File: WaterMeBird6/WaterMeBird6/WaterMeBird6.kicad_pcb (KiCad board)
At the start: 2 copper layers, 13 parts, among them J2 Conn_01x03, Q1 2N3904, SW1 SW_Push, U1 ATtiny85V-10P

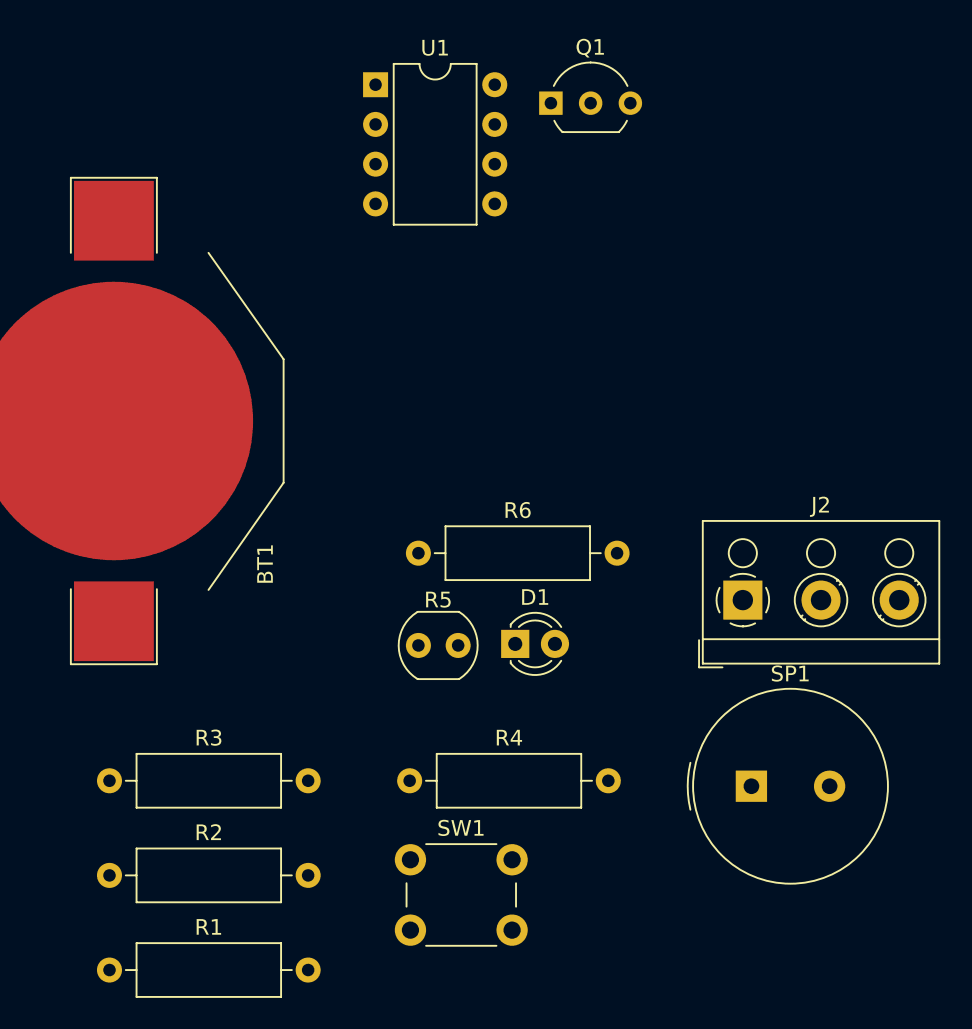
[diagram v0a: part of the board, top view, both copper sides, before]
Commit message: Added 'thick' version of footprints
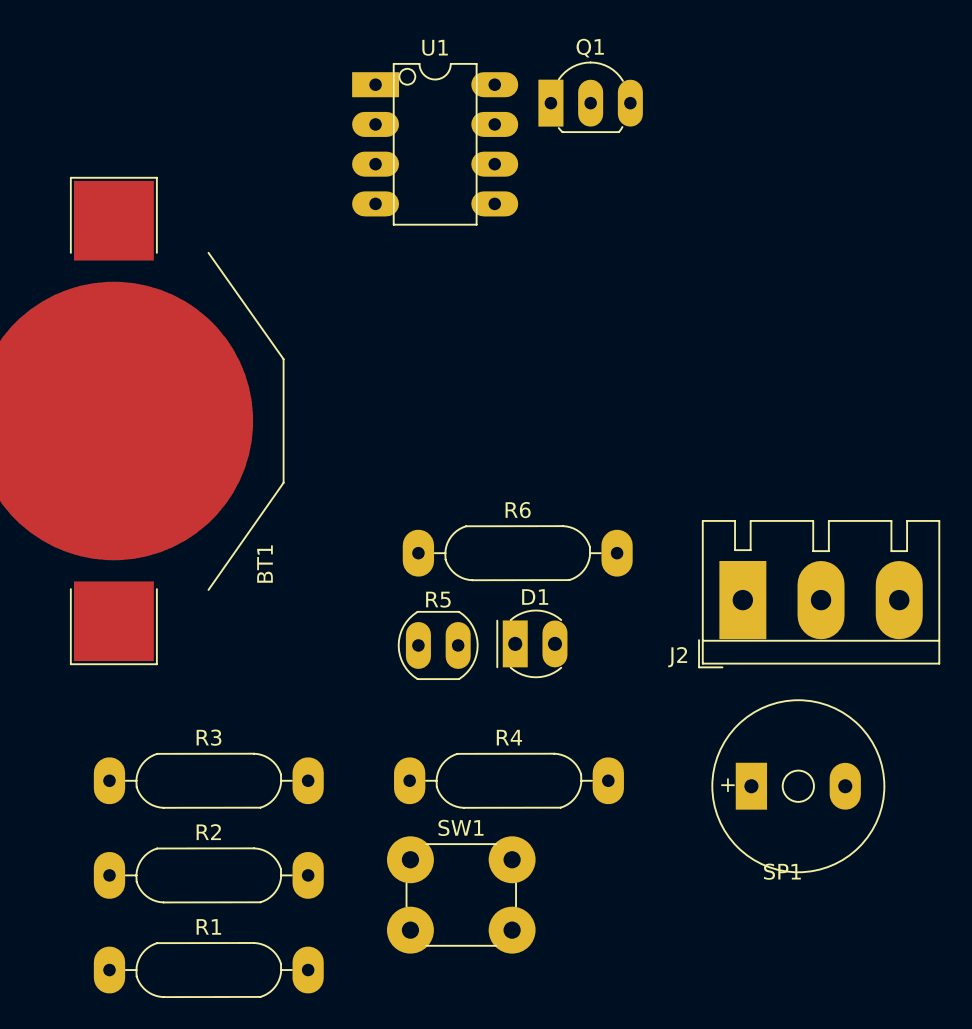
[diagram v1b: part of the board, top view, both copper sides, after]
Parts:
- D1: footprint LED_THT:LED_D3.0mm -> _Tinker:LED_D3.0mm_Thick
- J2: footprint TerminalBlock_RND:TerminalBlock_RND_205-00002_1x03_P5.00mm_Horizontal -> _Tinker:TerminalBlock_1x03_P5.00mm_Thick
- Q1: footprint Package_TO_SOT_THT:TO-92_Inline_Wide -> _Tinker:TO-92_Inline_Wide_Thick
- R1, R2, R3, R4, R6: footprint Resistor_THT:R_Axial_DIN0309_L9.0mm_D3.2mm_P12.70mm_Horizontal -> _Tinker:R_Axial_DIN0309_L9.0mm_D3.2mm_P12.70mm_Horizontal_Thick
- R5: footprint OptoDevice:R_LDR_4.9x4.2mm_P2.54mm_Vertical -> _Tinker:R_LDR_4.9x4.2mm_P2.54mm_Vertical_Thick
- SP1: footprint Buzzer_Beeper:Buzzer_TDK_PS1240P02BT_D12.2mm_H6.5mm -> _Tinker:MagneticBuzzer_Thick
- SW1: footprint Button_Switch_THT:SW_PUSH_6mm_H5mm -> _Tinker:SW_PUSH_6mm_H5mm_Thick
- U1: footprint Package_DIP:DIP-8_W7.62mm -> _Tinker:DIP-8_W7.62mm_Thick

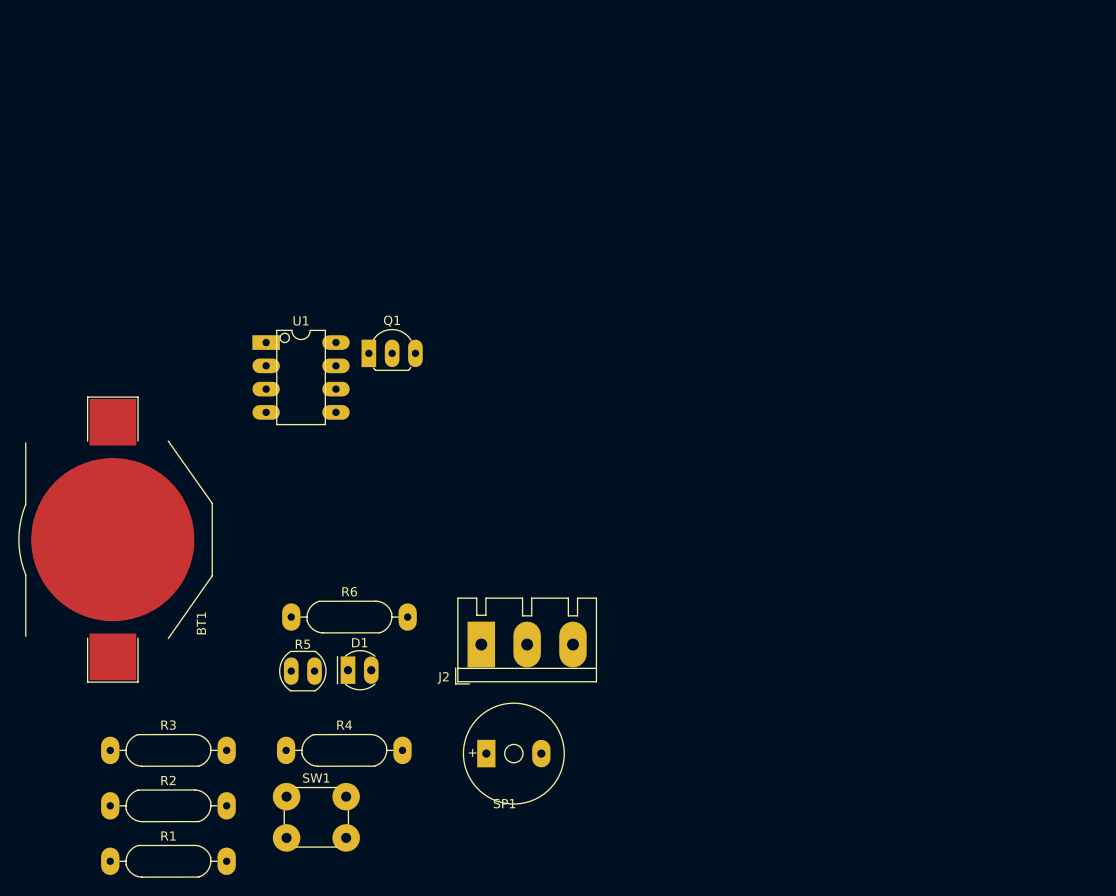
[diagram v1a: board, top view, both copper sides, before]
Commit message: added outline and placed
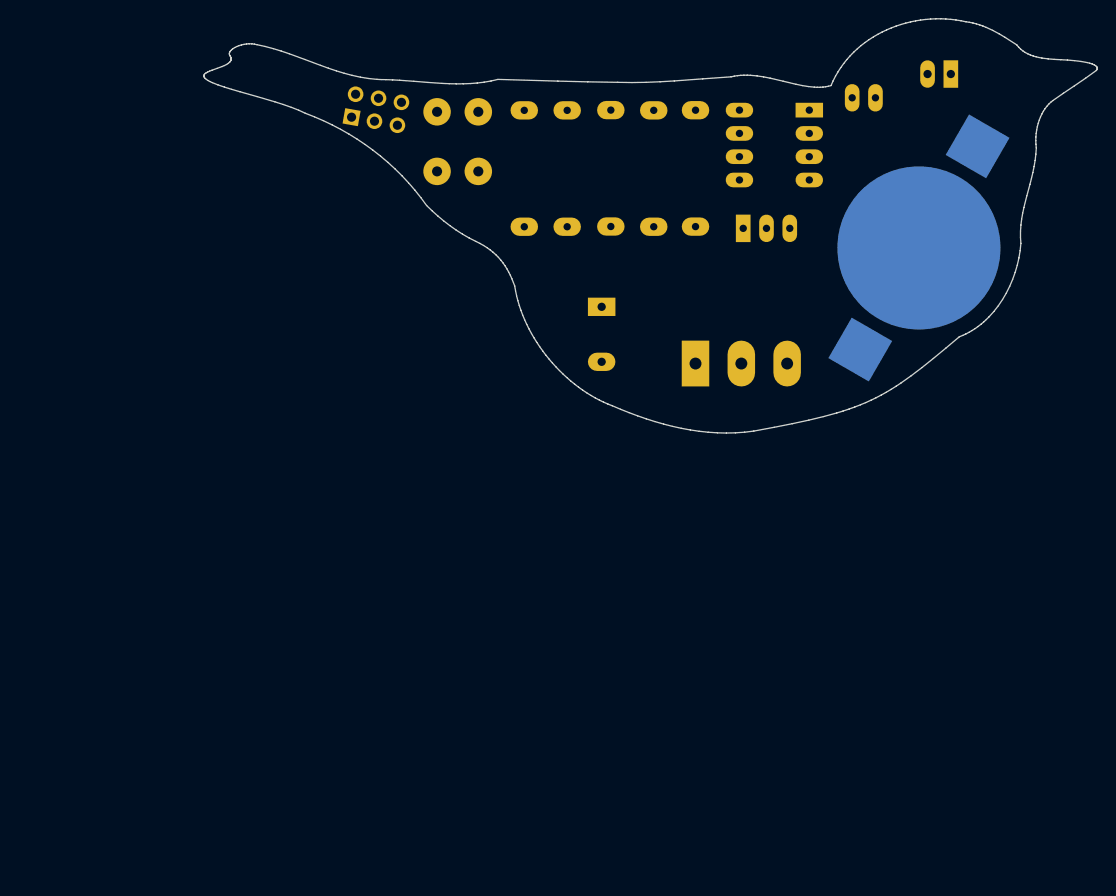
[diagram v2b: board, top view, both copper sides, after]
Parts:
- added J1: Conn_02x03_Odd_Even, Connector_PinSocket_2.54mm:PinSocket_2x03_P2.54mm_Vertical, B.Cu at (155.6, 68.2)
- added U2: outline, _Bird:bird_outline, F.Cu at (188.0, 106.7)
- BT1, D1, J2, Q1, R1, R2, R3, R4, R5, R6, SP1, SW1, U1: moved to B.Cu
- moved R1 93.6 mm to (174.4, 67.5), turned to -90 degrees
- moved BT1 93.5 mm to (217.5, 82.5), turned to 60 degrees
- moved D1 92.5 mm to (221.0, 63.5), turned to 180 degrees
- moved R2 90.8 mm to (179.1, 67.5), turned to -90 degrees
- moved R5 89.3 mm to (212.8, 66.1), turned to 180 degrees
- moved R3 88.7 mm to (183.9, 67.4), turned to -90 degrees
- moved R4 80.5 mm to (188.6, 67.5), turned to -90 degrees
- moved SW1 76.5 mm to (164.9, 67.6), turned to -90 degrees
- moved U1 64.5 mm to (205.5, 67.4), turned to 180 degrees
- moved R6 61.3 mm to (193.1, 80.1), turned to 90 degrees
- moved SP1 50.3 mm to (182.9, 88.9), turned to -90 degrees
- moved Q1 43.1 mm to (198.3, 80.3)
- moved J2 38.6 mm to (193.1, 95.1)
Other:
- board outline added: 97.5 x 45.2 mm
